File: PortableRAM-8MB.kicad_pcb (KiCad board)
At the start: 4 copper layers, 123 x 81 mm, 38 parts, among them J1 RAM Connector, J2 JTAG_Header_2.54mm_1x06, U1 ATF1502ASL, U11 74HC245, U12 74HC245, U2 AS6C8008-55TIN, U3 AS6C8008-55TIN, U4 AS6C8008-55TIN, U5 AS6C8008-55TIN, U6 AS6C8008-55TIN, U7 AS6C8008-55TIN, U8 AS6C8008-55TIN, U9 AS6C8008-55TIN

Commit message: Apply v0.3 silkscreen improvements to v2: cap values on B.SilkS, J2 JTAG labels
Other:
- board text added: "GND"
- board text added: "TCK"
- board text added: "TDI"
- board text added: "TDO"
- board text added: "TMS"
- board text added: "VCC"
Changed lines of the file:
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@@
 		(property "Value" "10µF"
 			(at 0 -1.68 0)
-			(layer "B.Fab")
-			(hide yes)
+			(layer "B.SilkS")
 			(effects
 				(font
-					(size 1 1)
+					(size 0.8 0.8)
 					(thickness 0.15)
 				)
@@
 		(property "Value" "100nF"
 			(at 0 -1.68 90)
-			(layer "B.Fab")
-			(hide yes)
+			(layer "B.SilkS")
 			(effects
 				(font
-					(size 1 1)
+					(size 0.8 0.8)
 					(thickness 0.15)
 				)
@@
 		(property "Value" "100nF"
 			(at 1.03723 -10.005847 0)
-			(layer "B.Fab")
-			(hide yes)
+			(layer "B.SilkS")
 			(effects
 				(font
-					(size 1 1)
+					(size 0.8 0.8)
 					(thickness 0.15)
 				)
@@
 		(property "Value" "100nF"
 			(at 1.03723 -10.005847 0)
-			(layer "B.Fab")
-			(hide yes)
+			(layer "B.SilkS")
 			(effects
 				(font
-					(size 1 1)
+					(size 0.8 0.8)
 					(thickness 0.15)
 				)
@@
 		(property "Value" "100nF"
 			(at 1.03723 -10.005847 90)
-			(layer "B.Fab")
-			(hide yes)
+			(layer "B.SilkS")
 			(effects
 				(font
-					(size 1 1)
+					(size 0.8 0.8)
 					(thickness 0.15)
 				)
@@
 		(property "Value" "100nF"
 			(at 1.03723 -10.005847 90)
-			(layer "B.Fab")
-			(hide yes)
+			(layer "B.SilkS")
 			(effects
 				(font
-					(size 1 1)
+					(size 0.8 0.8)
 					(thickness 0.15)
 				)
@@
 		(property "Value" "100nF"
 			(at 1.03723 -10.005847 90)
-			(layer "B.Fab")
-			(hide yes)
+			(layer "B.SilkS")
 			(effects
 				(font
-					(size 1 1)
+					(size 0.8 0.8)
 					(thickness 0.15)
 				)
@@
 		(property "Value" "100nF"
 			(at 1.03723 -10.005847 90)
-			(layer "B.Fab")
-			(hide yes)
+			(layer "B.SilkS")
 			(effects
 				(font
-					(size 1 1)
+					(size 0.8 0.8)
 					(thickness 0.15)
 				)
@@
 		(property "Value" "10µF"
 			(at 1.03723 -10.005847 0)
-			(layer "B.Fab")
-			(hide yes)
+			(layer "B.SilkS")
 			(effects
 				(font
-					(size 1 1)
+					(size 0.8 0.8)
 					(thickness 0.15)
 				)
@@
 		(property "Value" "100nF"
 			(at 1.03723 -10.005847 0)
-			(layer "B.Fab")
-			(hide yes)
+			(layer "B.SilkS")
 			(effects
 				(font
-					(size 1 1)
+					(size 0.8 0.8)
 					(thickness 0.15)
 				)
@@
 		(property "Value" "100nF"
 			(at 1.03723 -10.005847 90)
-			(layer "B.Fab")
-			(hide yes)
+			(layer "B.SilkS")
 			(effects
 				(font
-					(size 1 1)
+					(size 0.8 0.8)
 					(thickness 0.15)
 				)
@@
 		(property "Value" "100nF"
 			(at 1.03723 -10.005847 90)
-			(layer "B.Fab")
-			(hide yes)
+			(layer "B.SilkS")
 			(effects
 				(font
-					(size 1 1)
+					(size 0.8 0.8)
 					(thickness 0.15)
 				)
@@
 		(property "Value" "100nF"
 			(at 1.03723 -10.005847 90)
-			(layer "B.Fab")
-			(hide yes)
+			(layer "B.SilkS")
 			(effects
 				(font
-					(size 1 1)
+					(size 0.8 0.8)
 					(thickness 0.15)
 				)
@@
 		(property "Value" "10µF"
 			(at 1.03723 -10.005847 0)
-			(layer "B.Fab")
-			(hide yes)
+			(layer "B.SilkS")
 			(effects
 				(font
-					(size 1 1)
+					(size 0.8 0.8)
 					(thickness 0.15)
 				)
@@
 		(property "Value" "100nF"
 			(at 18.87473 -1.205847 0)
-			(layer "B.Fab")
-			(hide yes)
+			(layer "B.SilkS")
 			(effects
 				(font
-					(size 1 1)
+					(size 0.8 0.8)
 					(thickness 0.15)
 				)
@@
 		(property "Value" "10µF"
 			(at 1.03723 -10.005847 0)
-			(layer "B.Fab")
-			(hide yes)
+			(layer "B.SilkS")
 			(effects
 				(font
-					(size 1 1)
+					(size 0.8 0.8)
 					(thickness 0.15)
 				)
@@
 		(property "Value" "100nF"
 			(at 1.03723 -10.005847 90)
-			(layer "B.Fab")
-			(hide yes)
+			(layer "B.SilkS")
 			(effects
 				(font
-					(size 1 1)
+					(size 0.8 0.8)
 					(thickness 0.15)
 				)
@@
 		(property "Value" "10µF"
 			(at 1.03723 -10.005847 0)
-			(layer "B.Fab")
-			(hide yes)
+			(layer "B.SilkS")
 			(effects
 				(font
-					(size 1 1)
+					(size 0.8 0.8)
 					(thickness 0.15)
 				)
@@
 		(property "Value" "100nF"
 			(at 1.03723 -10.005847 90)
-			(layer "B.Fab")
-			(hide yes)
+			(layer "B.SilkS")
 			(effects
 				(font
-					(size 1 1)
+					(size 0.8 0.8)
 					(thickness 0.15)
 				)
@@
 	)
 	(embedded_fonts no)
+	(gr_text "1"
+		(at 156.5 131.8)
+		(layer "F.SilkS")
+		(effects
+			(font
+				(size 0.8 0.8)
+				(thickness 0.12)
+			)
+		)
+	)
+	(gr_text "TCK"
+		(at 156.5 133.2)
+		(layer "F.SilkS")
+		(effects
+			(font
+				(size 0.8 0.8)
+				(thickness 0.12)
+			)
+		)
+	)
+	(gr_text "TMS"
+		(at 159.04 133.2)
+		(layer "F.SilkS")
+		(effects
+			(font
+				(size 0.8 0.8)
+				(thickness 0.12)
+			)
+		)
+	)
+	(gr_text "TDI"
+		(at 161.58 133.2)
+		(layer "F.SilkS")
+		(effects
+			(font
+				(size 0.8 0.8)
+				(thickness 0.12)
+			)
+		)
+	)
+	(gr_text "TDO"
+		(at 164.12 133.2)
+		(layer "F.SilkS")
+		(effects
+			(font
+				(size 0.8 0.8)
+				(thickness 0.12)
+			)
+		)
+	)
+	(gr_text "VCC"
+		(at 166.66 133.2)
+		(layer "F.SilkS")
+		(effects
+			(font
+				(size 0.8 0.8)
+				(thickness 0.12)
+			)
+		)
+	)
+	(gr_text "GND"
+		(at 169.2 133.2)
+		(layer "F.SilkS")
+		(effects
+			(font
+				(size 0.8 0.8)
+				(thickness 0.12)
+			)
+		)
+	)
 )

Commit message: Add silkscreen population guide boxes — 4MB (JP1 CLOSED) and 8MB ONLY (JP1 OPEN)
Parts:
- U2: value AS6C8008-55TIN -> AS6C8008-55ZIN
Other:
- board text added: "4MB"
- board text added: "8MB ONLY"
- board text added: "JP1 CLOSED"
- board text added: "JP1 OPEN"
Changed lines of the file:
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@@
 		(property "Value" "74HC245"
 			(at 0 3 90)
-			(layer "F.Fab")
+			(layer "F.SilkS")
 			(effects
 				(font
@@
 		(tags "TQFP QFP Microchip_44-Lead-Plastic-Thin-Quad-Flatpack-(PT)")
 		(property "Reference" "U1"
-			(at 0 0.5 90)
+			(at -3.5 -7.6625 90)
 			(layer "F.SilkS")
 			(effects
@@
 		(property "Value" "ATF1502ASL"
 			(at 0.5 -2.5 90)
-			(layer "F.Fab")
+			(layer "F.SilkS")
 			(effects
 				(font
@@
 			)
 		)
-		(property "Value" "AS6C8008-55TIN"
+		(property "Value" "AS6C8008-55ZIN"
 			(at -2.5 0 90)
-			(layer "F.Fab")
+			(layer "F.SilkS")
 			(effects
 				(font
@@
 		(property "Value" "RAM Connector"
 			(at -0.5 7.5 0)
-			(layer "F.Fab")
+			(layer "F.SilkS")
 			(effects
 				(font
@@
 		(property "Value" "74HC245"
 			(at 0 3 90)
-			(layer "F.Fab")
+			(layer "F.SilkS")
 			(effects
 				(font
@@
 		)
 		(property "Value" "100nF"
-			(at 0 -1.68 90)
+			(at -3 -2 90)
 			(layer "B.SilkS")
 			(effects
@@
 		)
 		(property "Value" "100nF"
-			(at 1.03723 -10.005847 0)
+			(at -3.5 -2.5 0)
 			(layer "B.SilkS")
 			(effects
@@
 		)
 		(property "Value" "100nF"
-			(at 1.03723 -10.005847 0)
+			(at -3.73 -3 0)
 			(layer "B.SilkS")
 			(effects
@@
 		)
 		(property "Value" "100nF"
-			(at 1.03723 -10.005847 90)
+			(at -3 -2.0875 90)
 			(layer "B.SilkS")
 			(effects
@@
 		)
 		(property "Value" "100nF"
-			(at 1.03723 -10.005847 90)
+			(at -3.5 -2 90)
 			(layer "B.SilkS")
 			(effects
@@
 		)
 		(property "Value" "100nF"
-			(at 1.03723 -10.005847 90)
+			(at -3 -1.5875 90)
 			(layer "B.SilkS")
 			(effects
@@
 		)
 		(property "Value" "100nF"
-			(at 1.03723 -10.005847 90)
+			(at -2.5 -2.0875 90)
 			(layer "B.SilkS")
 			(effects
@@
 		)
 		(property "Value" "10µF"
-			(at 1.03723 -10.005847 0)
+			(at -4 -2 0)
 			(layer "B.SilkS")
 			(effects
@@
 		)
 		(property "Value" "100nF"
-			(at 1.03723 -10.005847 0)
+			(at -3.23 -2 0)
 			(layer "B.SilkS")
 			(effects
@@
 		)
 		(property "Value" "100nF"
-			(at 1.03723 -10.005847 90)
+			(at -3 -2.0875 90)
 			(layer "B.SilkS")
 			(effects
@@
 		)
 		(property "Value" "100nF"
-			(at 1.03723 -10.005847 90)
+			(at -3.5 -2.0875 90)
 			(layer "B.SilkS")
 			(effects
@@
 		)
 		(property "Value" "100nF"
-			(at 1.03723 -10.005847 90)
+			(at -2.5 -2.0875 90)
 			(layer "B.SilkS")
 			(effects
@@
 		)
 		(property "Value" "10µF"
-			(at 1.03723 -10.005847 0)
+			(at -4.0875 -2 0)
 			(layer "B.SilkS")
 			(effects
@@
 		)
 		(property "Value" "100nF"
-			(at 18.87473 -1.205847 0)
+			(at -2.5 -1.5 0)
 			(layer "B.SilkS")
 			(effects
@@
 		)
 		(property "Value" "10µF"
-			(at 1.03723 -10.005847 0)
+			(at -3.5875 -1.5 0)
 			(layer "B.SilkS")
 			(effects
@@
 		)
 		(property "Value" "100nF"
-			(at 1.03723 -10.005847 90)
+			(at -2.95 -2.0875 90)
 			(layer "B.SilkS")
 			(effects
@@
 		)
 		(property "Value" "10µF"
-			(at 1.03723 -10.005847 0)
+			(at -3.5 -2.5 0)
 			(layer "B.SilkS")
 			(effects
@@
 		)
 		(property "Value" "100nF"
-			(at 1.03723 -10.005847 90)
+			(at -3 -1.5875 90)
 			(layer "B.SilkS")
 			(effects
@@
 		(layer "Edge.Cuts")
 	)
+	(gr_text "GND"
+		(at 144 133 0)
+		(layer "F.SilkS")
+		(effects
+			(font
+				(size 0.8 0.8)
+				(thickness 0.12)
+			)
+		)
+	)
+	(gr_text "VCC"
+		(at 146.5 133 0)
+		(layer "F.SilkS")
+		(effects
+			(font
+				(size 0.8 0.8)
+				(thickness 0.12)
+			)
+		)
+	)
+	(gr_text "TDO"
+		(at 149 133 0)
+		(layer "F.SilkS")
+		(effects
+			(font
+				(size 0.8 0.8)
+				(thickness 0.12)
+			)
+		)
+	)
+	(gr_text "TDI"
+		(at 151.5 133 0)
+		(layer "F.SilkS")
+		(effects
+			(font
+				(size 0.8 0.8)
+				(thickness 0.12)
+			)
+		)
+	)
+	(gr_text "TMS"
+		(at 154 133 0)
+		(layer "F.SilkS")
+		(effects
+			(font
+				(size 0.8 0.8)
+				(thickness 0.12)
+			)
+		)
+	)
+	(gr_text "1"
+		(at 156.5 131.8 0)
+		(layer "F.SilkS")
+		(effects
+			(font
+				(size 0.8 0.8)
+				(thickness 0.12)
+			)
+		)
+	)
+	(gr_text "TCK"
+		(at 156.5 133.2 0)
+		(layer "F.SilkS")
+		(effects
+			(font
+				(size 0.8 0.8)
+				(thickness 0.12)
+			)
+		)
+	)
 	(gr_text "4+8MB"
 		(at 113.4125 98.1 0)
@@
 	)
 	(embedded_fonts no)
-	(gr_text "1"
-		(at 156.5 131.8)
-		(layer "F.SilkS")
-		(effects
-			(font
-				(size 0.8 0.8)
-				(thickness 0.12)
-			)
+	(gr_rect
+		(start 105.5 77.5)
+		(end 142.5 121.5)
+		(stroke
+			(width 0.2)
+			(type default)
 		)
-	)
-	(gr_text "TCK"
-		(at 156.5 133.2)
+		(fill none)
 		(layer "F.SilkS")
-		(effects
-			(font
-				(size 0.8 0.8)
-				(thickness 0.12)
-			)
-		)
 	)
-	(gr_text "TMS"
-		(at 159.04 133.2)
+	(gr_text "4MB"
+		(at 124.0 79.3)
 		(layer "F.SilkS")
 		(effects
 			(font
-				(size 0.8 0.8)
-				(thickness 0.12)
+				(size 1.2 1.2)
+				(thickness 0.18)
 			)
 		)
 	)
-	(gr_text "TDI"
-		(at 161.58 133.2)
+	(gr_text "JP1 CLOSED"
+		(at 124.0 80.9)
 		(layer "F.SilkS")
 		(effects
@@
 		)
 	)
-	(gr_text "TDO"
-		(at 164.12 133.2)
-		(layer "F.SilkS")
-		(effects
-			(font
-				(size 0.8 0.8)
-				(thickness 0.12)
-			)
+	(gr_rect
+		(start 148.5 77.5)
+		(end 186.5 121.5)
+		(stroke
+			(width 0.2)
+			(type default)
 		)
+		(fill none)
+		(layer "F.SilkS")
 	)
-	(gr_text "VCC"
-		(at 166.66 133.2)
+	(gr_text "8MB ONLY"
+		(at 167.5 79.3)
 		(layer "F.SilkS")
 		(effects
 			(font
-				(size 0.8 0.8)
-				(thickness 0.12)
+				(size 1.2 1.2)
+				(thickness 0.18)
 			)
 		)
 	)
-	(gr_text "GND"
-		(at 169.2 133.2)
+	(gr_text "JP1 OPEN"
+		(at 167.5 80.9)
 		(layer "F.SilkS")
 		(effects

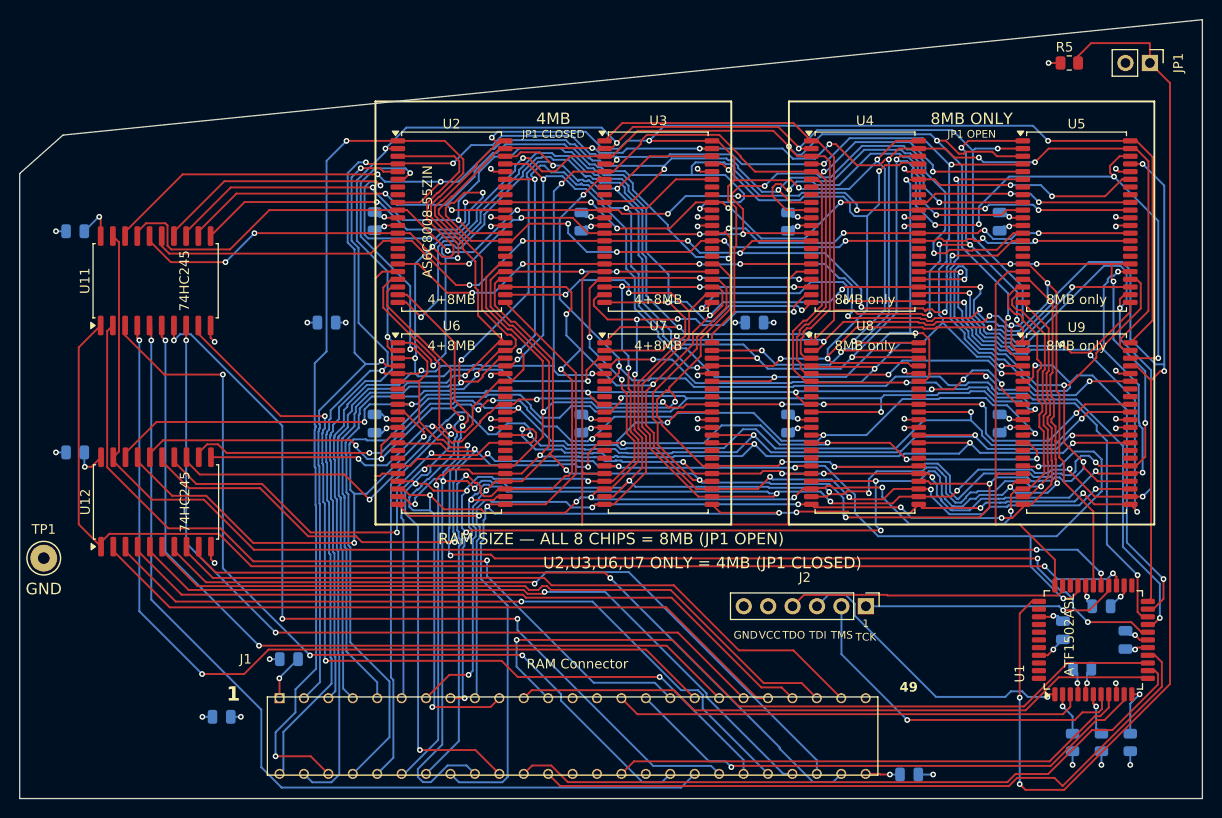
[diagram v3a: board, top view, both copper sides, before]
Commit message: Regenerate Gerbers for v2.0 — cap silkscreen, J2 labels, population boxes, rev 2.0
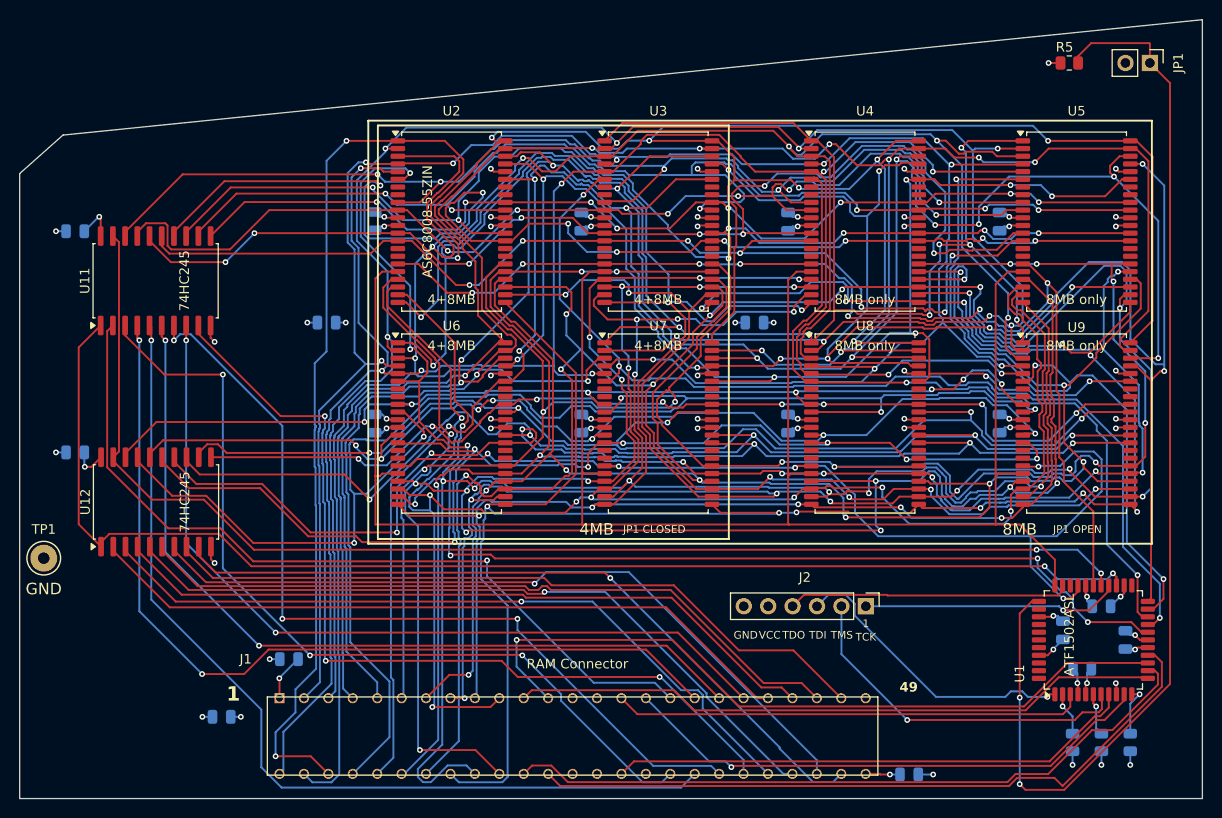
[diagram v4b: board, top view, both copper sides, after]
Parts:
- JP1: value SIZE: open=8MB closed=4MB -> JP1: open=8MB closed=4MB
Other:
- board text added: "8MB"
- board text removed: "8MB ONLY"
- board text removed: "RAM SIZE — ALL 8 CHIPS = 8MB (JP1 OPEN)"
- board text removed: "U2,U3,U6,U7 ONLY = 4MB (JP1 CLOSED)"
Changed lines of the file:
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@@
 		(tags "TSOP-II SO")
 		(property "Reference" "U2"
-			(at 0 -10.16 0)
+			(at 0 -11.5 0)
 			(layer "F.SilkS")
 			(effects
@@
 		(tags "TSOP-II SO")
 		(property "Reference" "U3"
-			(at 0 -10.5 180)
+			(at 0 -11.5 180)
 			(layer "F.SilkS")
 			(effects
@@
 		(tags "TSOP-II SO")
 		(property "Reference" "U4"
-			(at 0 -10.5 180)
+			(at 0 -11.5 180)
 			(layer "F.SilkS")
 			(effects
@@
 			)
 		)
-		(property "Value" "SIZE: open=8MB closed=4MB"
+		(property "Value" "JP1: open=8MB closed=4MB"
 			(at 3.5 7 0)
 			(layer "F.Fab")
@@
 		(tags "TSOP-II SO")
 		(property "Reference" "U5"
-			(at 0 -10.16 0)
+			(at 0 -11.5 0)
 			(layer "F.SilkS")
 			(effects
@@
 		)
 	)
+	(gr_rect
+		(start 104.75 79.5)
+		(end 186.25 123.5)
+		(stroke
+			(width 0.2)
+			(type default)
+		)
+		(fill no)
+		(layer "F.SilkS")
+	)
+	(gr_rect
+		(start 105.75 80)
+		(end 142.25 123)
+		(stroke
+			(width 0.2)
+			(type default)
+		)
+		(fill no)
+		(layer "F.SilkS")
+	)
 	(gr_poly
 		(pts
@@
 		(layer "Edge.Cuts")
 	)
+	(gr_text "JP1 CLOSED"
+		(at 134.5 122 0)
+		(layer "F.SilkS")
+		(effects
+			(font
+				(size 0.8 0.8)
+				(thickness 0.12)
+			)
+		)
+	)
 	(gr_text "GND"
 		(at 144 133 0)
@@
 		)
 	)
+	(gr_text "JP1 OPEN"
+		(at 178.5 122 0)
+		(layer "F.SilkS")
+		(effects
+			(font
+				(size 0.8 0.8)
+				(thickness 0.12)
+			)
+		)
+	)
 	(gr_text "4+8MB"
 		(at 113.4125 98.1 0)
@@
 		)
 	)
-	(gr_text "RAM SIZE — ALL 8 CHIPS = 8MB (JP1 OPEN)"
-		(at 130 123 0)
+	(gr_text "4MB"
+		(at 128.5 122 0)
 		(layer "F.SilkS")
 		(effects
 			(font
 				(size 1.2 1.2)
-				(thickness 0.15)
+				(thickness 0.18)
 			)
 		)
 	)
-	(gr_text "U2,U3,U6,U7 ONLY = 4MB (JP1 CLOSED)"
-		(at 139.5 125.5 0)
+	(gr_text "8MB"
+		(at 172.5 122 0)
 		(layer "F.SilkS")
 		(effects
 			(font
 				(size 1.2 1.2)
-				(thickness 0.15)
+				(thickness 0.18)
 			)
 		)
@@
 	)
 	(embedded_fonts no)
-	(gr_rect
-		(start 105.5 77.5)
-		(end 142.5 121.5)
-		(stroke
-			(width 0.2)
-			(type default)
-		)
-		(fill none)
-		(layer "F.SilkS")
-	)
-	(gr_text "4MB"
-		(at 124.0 79.3)
-		(layer "F.SilkS")
-		(effects
-			(font
-				(size 1.2 1.2)
-				(thickness 0.18)
-			)
-		)
-	)
-	(gr_text "JP1 CLOSED"
-		(at 124.0 80.9)
-		(layer "F.SilkS")
-		(effects
-			(font
-				(size 0.8 0.8)
-				(thickness 0.12)
-			)
-		)
-	)
-	(gr_rect
-		(start 148.5 77.5)
-		(end 186.5 121.5)
-		(stroke
-			(width 0.2)
-			(type default)
-		)
-		(fill none)
-		(layer "F.SilkS")
-	)
-	(gr_text "8MB ONLY"
-		(at 167.5 79.3)
-		(layer "F.SilkS")
-		(effects
-			(font
-				(size 1.2 1.2)
-				(thickness 0.18)
-			)
-		)
-	)
-	(gr_text "JP1 OPEN"
-		(at 167.5 80.9)
-		(layer "F.SilkS")
-		(effects
-			(font
-				(size 0.8 0.8)
-				(thickness 0.12)
-			)
-		)
-	)
 )
